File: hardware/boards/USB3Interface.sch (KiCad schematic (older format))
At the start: 6 parts, among them J2 USB3_Micro_B_Amphenol, U1 ECP5UM5G-381caBGA, U3 CYUSB3014, U6 128MiB

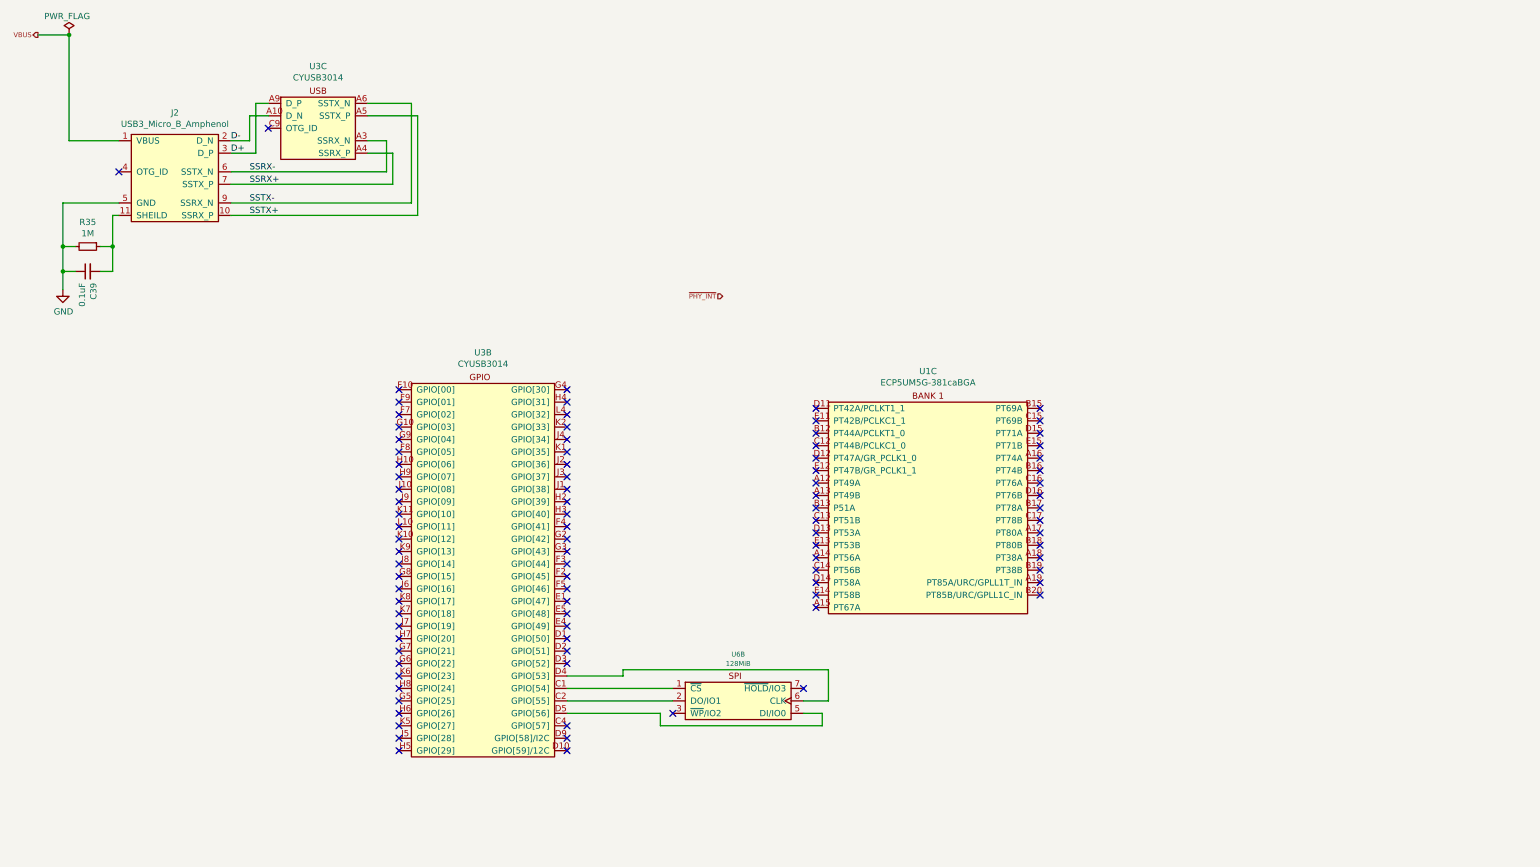
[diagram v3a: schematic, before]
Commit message: Added headers for the SPI flash for both the FPGA and the PHY
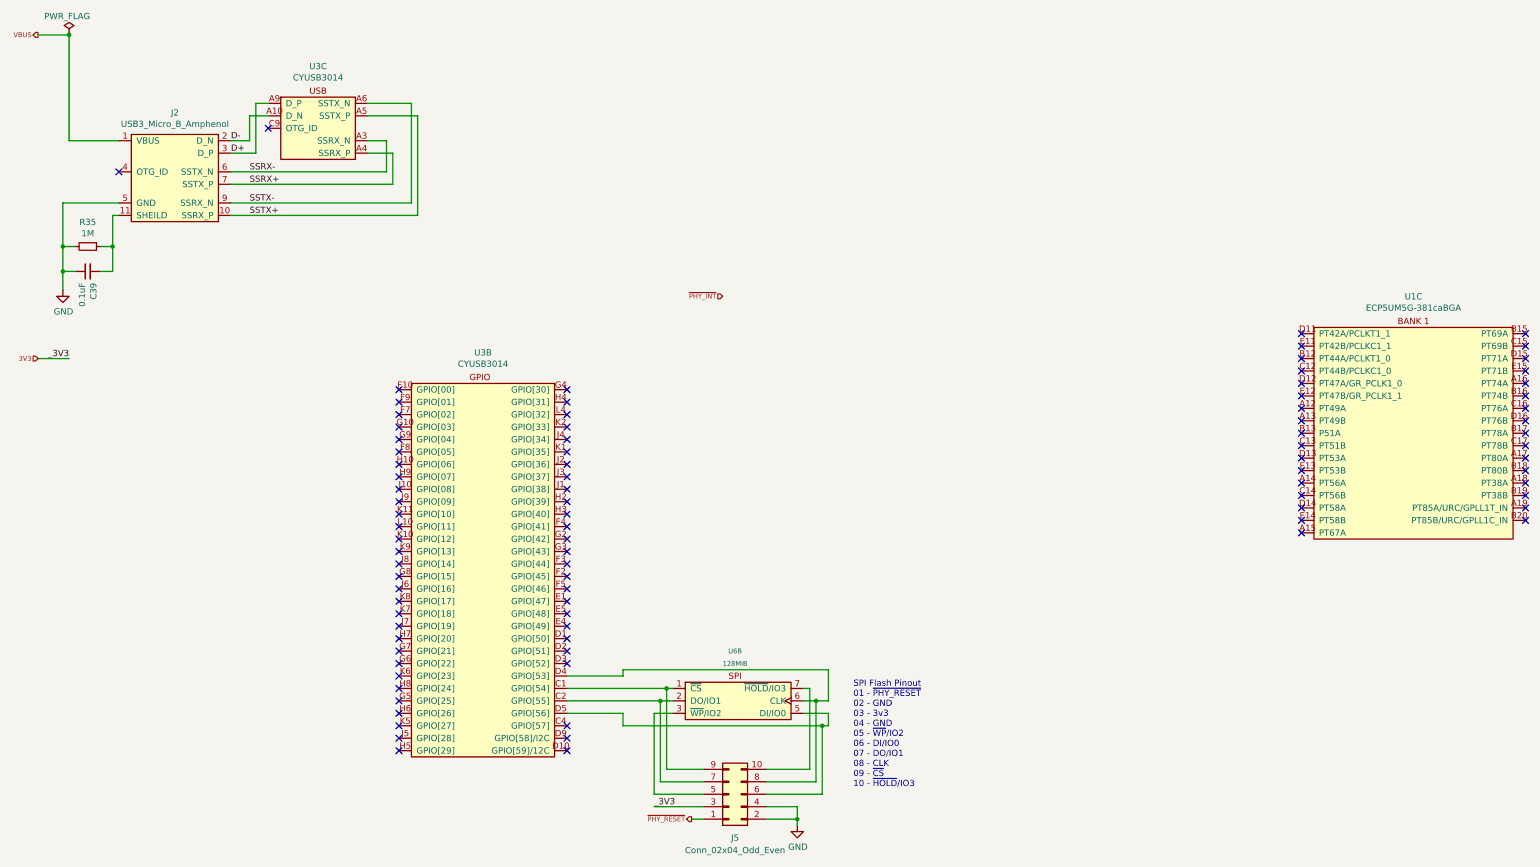
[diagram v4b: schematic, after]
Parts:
- added J5: Conn_02x04_Odd_Even, Connector_PinHeader_1.27mm:PinHeader_2x05_P1.27mm_Vertical, symbol Connector_Generic:Conn_02x05_Odd_Even
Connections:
- net GND: now also J5.2 (Pin_2), J5.4 (Pin_4)
- net at U3.C1 (GPIO[54]), U6.1 (~CS): now also J5.9 (Pin_9)
- net at U3.C2 (GPIO[55]), U6.2 (DO/IO1): now also J5.7 (Pin_7)
- net at U3.D4 (GPIO[53]), U6.6 (CLK): now also J5.8 (Pin_8)
- net at U3.D5 (GPIO[56]), U6.5 (DI/IO0): now also J5.6 (Pin_6)
- net at U6.3 (~WP~/IO2): now also J5.5 (Pin_5)
- net at U6.7 (~HOLD~/IO3): now also J5.10 (Pin_10)
- new net 3V3: J5.3 (Pin_3)
- new net ~PHY_RESET: J5.1 (Pin_1)
- no-connect marks 93 -> 91
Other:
- note added: "SPI Flash Pinout\n01 - ~PHY_RESET~\n02 - GND\n03 - 3v3\n04 - GND\n05 - ~WP~/IO2\n06 - DI/IO0\n07 - DO/IO1\n08 - CLK\n09 - ~CS~\n10 - ~HOLD~/IO3\n"
- moved on the sheet: U1C
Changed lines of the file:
@@
 L lethalbit:ECP5UM5G-381caBGA U?
 U 3 1 5F2EB784
-P 7950 3750
+P 11850 3150
 AR Path="/5F2EB784" Ref="U?"  Part="3"
 AR Path="/5F2CAFD2/5F2EB784" Ref="U1"  Part="3"
-F 0 "U1" H 7950 4098 50  0000 C CNN
-F 1 "ECP5UM5G-381caBGA" H 7950 4007 50  0000 C CNN
-F 2 "lethalbit:318caBGA" H 6600 3900 50  0001 C CNN
-F 3 "" H 6600 3900 50  0001 C CNN
-F 4 "Lattice" H 7950 3750 50  0001 C CNN "MFR"
-F 5 "LFE5UM5G-85F-8BG381I" H 7950 3750 50  0001 C CNN "MPN"
-F 6 "220-2112-ND" H 7950 3750 50  0001 C CNN "DIGIKEY_PN"
-	3    7950 3750
+F 0 "U1" H 11850 3498 50  0000 C CNN
+F 1 "ECP5UM5G-381caBGA" H 11850 3407 50  0000 C CNN
+F 2 "lethalbit:318caBGA" H 10500 3300 50  0001 C CNN
+F 3 "" H 10500 3300 50  0001 C CNN
+F 4 "Lattice" H 11850 3150 50  0001 C CNN "MFR"
+F 5 "LFE5UM5G-85F-8BG381I" H 11850 3150 50  0001 C CNN "MPN"
+F 6 "220-2112-ND" H 11850 3150 50  0001 C CNN "DIGIKEY_PN"
+	3    11850 3150
 	1    0    0    -1
 $EndComp
@@
 NoConn ~ 5050 3650
 NoConn ~ 5050 3550
-NoConn ~ 7050 3700
-NoConn ~ 7050 3800
-NoConn ~ 7050 3900
-NoConn ~ 7050 4000
-NoConn ~ 7050 4100
-NoConn ~ 7050 4200
-NoConn ~ 7050 4300
-NoConn ~ 7050 4400
-NoConn ~ 7050 4500
-NoConn ~ 7050 4600
-NoConn ~ 7050 4800
-NoConn ~ 7050 4900
-NoConn ~ 7050 5000
-NoConn ~ 7050 5100
-NoConn ~ 7050 5200
-NoConn ~ 7050 5300
-NoConn ~ 8850 5200
-NoConn ~ 8850 5100
-NoConn ~ 8850 5000
-NoConn ~ 8850 4900
-NoConn ~ 8850 4800
-NoConn ~ 8850 4700
-NoConn ~ 8850 4600
-NoConn ~ 8850 4500
-NoConn ~ 8850 4400
-NoConn ~ 8850 4300
-NoConn ~ 8850 4200
-NoConn ~ 8850 4100
-NoConn ~ 8850 4000
-NoConn ~ 8850 3900
-NoConn ~ 8850 3800
-NoConn ~ 8850 3700
+NoConn ~ 10950 3100
+NoConn ~ 10950 3200
+NoConn ~ 10950 3300
+NoConn ~ 10950 3400
+NoConn ~ 10950 3500
+NoConn ~ 10950 3600
+NoConn ~ 10950 3700
+NoConn ~ 10950 3800
+NoConn ~ 10950 3900
+NoConn ~ 10950 4000
+NoConn ~ 10950 4200
+NoConn ~ 10950 4300
+NoConn ~ 10950 4400
+NoConn ~ 10950 4500
+NoConn ~ 10950 4600
+NoConn ~ 10950 4700
+NoConn ~ 12750 4600
+NoConn ~ 12750 4500
+NoConn ~ 12750 4400
+NoConn ~ 12750 4300
+NoConn ~ 12750 4200
+NoConn ~ 12750 4100
+NoConn ~ 12750 4000
+NoConn ~ 12750 3900
+NoConn ~ 12750 3800
+NoConn ~ 12750 3700
+NoConn ~ 12750 3600
+NoConn ~ 12750 3500
+NoConn ~ 12750 3400
+NoConn ~ 12750 3300
+NoConn ~ 12750 3200
+NoConn ~ 12750 3100
 Text HLabel 800  700  0    39   Output ~ 0
 VBUS
@@
 Wire Wire Line
 	3850 1350 3450 1350
-NoConn ~ 7050 4700
+NoConn ~ 10950 4100
 Text Label 2500 1800 0    50   ~ 0
 SSRX-
@@
 AR Path="/5EF66251/5FF1D42C" Ref="U?"  Part="2"
 AR Path="/5F2CAFD2/5FF1D42C" Ref="U6"  Part="2"
-F 0 "U6" H 6425 6124 39  0000 C CNN
-F 1 "128MiB" H 6425 6049 39  0000 C CNN
+F 0 "U6" H 6400 6150 39  0000 C CNN
+F 1 "128MiB" H 6400 6050 39  0000 C CNN
 F 2 "lethalbit-memory:WSON-8-1EP-6.0x8.0mm" H 6400 6050 39  0001 C CNN
 F 3 "https://www.winbond.com/resource-files/w25n01gv%20revl%20050918%20unsecured.pdf" H 6400 6050 39  0001 C CNN
@@
 $EndComp
 Wire Wire Line
-	6950 6050 7150 6050
+	6950 6050 7050 6050
 Wire Wire Line
 	7150 6050 7150 5800
@@
 	5500 5850 5050 5850
 Wire Wire Line
-	5900 5950 5050 5950
-Wire Wire Line
-	5900 6050 5050 6050
-Wire Wire Line
-	6950 6150 7100 6150
-Wire Wire Line
-	7100 6150 7100 6250
-Wire Wire Line
-	7100 6250 5800 6250
-Wire Wire Line
-	5800 6250 5800 6150
-Wire Wire Line
-	5800 6150 5050 6150
+	5900 5950 5850 5950
+Wire Wire Line
+	5900 6050 5800 6050
+Wire Wire Line
+	6950 6150 7150 6150
+Wire Wire Line
+	7150 6150 7150 6250
+Wire Wire Line
+	7150 6250 7100 6250
+Wire Wire Line
+	5500 6250 5500 6150
+Wire Wire Line
+	5500 6150 5050 6150
 $Comp
 L power:PWR_FLAG #FLG?
@@
 $EndComp
 Connection ~ 1050 700
-NoConn ~ 6950 5950
-NoConn ~ 5900 6150
 Text HLabel 6300 2800 0    39   Input ~ 0
 ~PHY_INT
+$Comp
+L Connector_Generic:Conn_02x05_Odd_Even J?
+U 1 1 60F06E66
+P 6350 6800
+AR Path="/5EF66251/60F06E66" Ref="J?"  Part="1"
+AR Path="/5F2CAFD2/60F06E66" Ref="J5"  Part="1"
+F 0 "J5" H 6400 7150 50  0000 C CNN
+F 1 "Conn_02x04_Odd_Even" H 6400 7250 50  0000 C CNN
+F 2 "Connector_PinHeader_1.27mm:PinHeader_2x05_P1.27mm_Vertical" H 6350 6800 50  0001 C CNN
+F 3 "~" H 6350 6800 50  0001 C CNN
+	1    6350 6800
+	1    0    0    1
+$EndComp
+Text Notes 7350 6750 0    50   ~ 0
+SPI Flash Pinout\n01 - ~PHY_RESET~\n02 - GND\n03 - 3v3\n04 - GND\n05 - ~WP~/IO2\n06 - DI/IO0\n07 - DO/IO1\n08 - CLK\n09 - ~CS~\n10 - ~HOLD~/IO3\n
+$Comp
+L power:GND #PWR0138
+U 1 1 60F24716
+P 6900 7050
+F 0 "#PWR0138" H 6900 6800 50  0001 C CNN
+F 1 "GND" H 6905 6877 50  0000 C CNN
+F 2 "" H 6900 7050 50  0001 C CNN
+F 3 "" H 6900 7050 50  0001 C CNN
+	1    6900 7050
+	1    0    0    -1
+$EndComp
+Text HLabel 6050 7000 0    39   Output ~ 0
+~PHY_RESET
+Wire Wire Line
+	6950 5950 7000 5950
+Wire Wire Line
+	7000 5950 7000 6600
+Wire Wire Line
+	7000 6600 6650 6600
+Wire Wire Line
+	7050 6050 7050 6700
+Wire Wire Line
+	7050 6700 6650 6700
+Connection ~ 7050 6050
+Wire Wire Line
+	7050 6050 7150 6050
+Wire Wire Line
+	7100 6250 7100 6800
+Wire Wire Line
+	7100 6800 6650 6800
+Connection ~ 7100 6250
+Wire Wire Line
+	7100 6250 5500 6250
+Wire Wire Line
+	6150 6600 5850 6600
+Wire Wire Line
+	5850 6600 5850 5950
+Connection ~ 5850 5950
+Wire Wire Line
+	5850 5950 5050 5950
+Wire Wire Line
+	5800 6050 5800 6700
+Wire Wire Line
+	5800 6700 6150 6700
+Connection ~ 5800 6050
+Wire Wire Line
+	5800 6050 5050 6050
+Wire Wire Line
+	5900 6150 5750 6150
+Wire Wire Line
+	5750 6150 5750 6800
+Wire Wire Line
+	5750 6800 6150 6800
+Wire Wire Line
+	6050 7000 6150 7000
+Wire Wire Line
+	6650 6900 6900 6900
+Wire Wire Line
+	6900 6900 6900 7000
+Wire Wire Line
+	6650 7000 6900 7000
+Connection ~ 6900 7000
+Wire Wire Line
+	6900 7000 6900 7050
+Wire Wire Line
+	6150 6900 5750 6900
+Text Label 5750 6900 0    50   ~ 0
+_3V3
+Text HLabel 800  3300 0    39   Input ~ 0
+3V3
+Wire Wire Line
+	800  3300 1050 3300
+Text Label 1050 3300 2    50   ~ 0
+_3V3
 $EndSCHEMATC

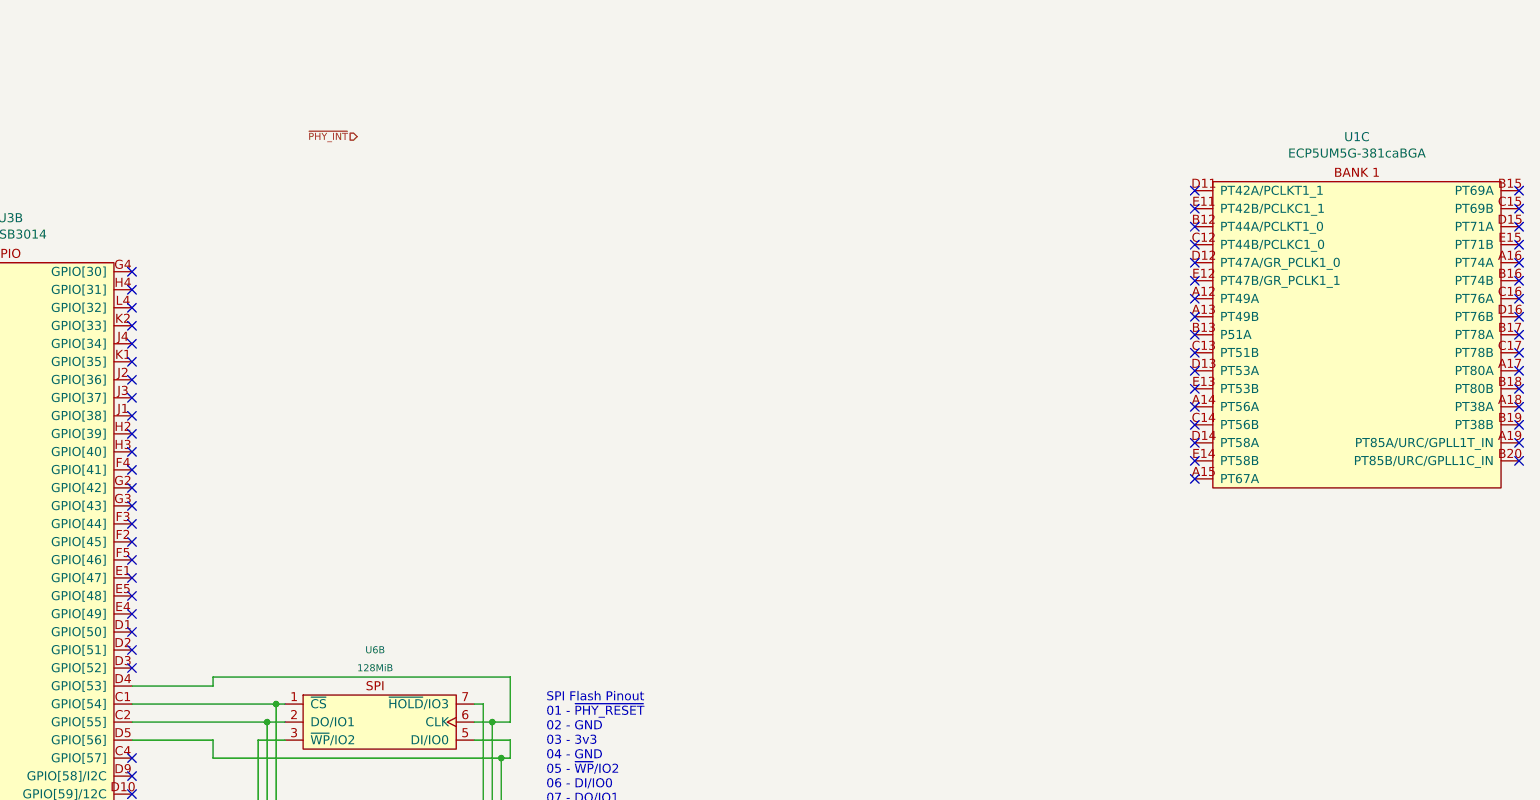
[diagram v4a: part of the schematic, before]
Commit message: Added the main OSC for the FPGA
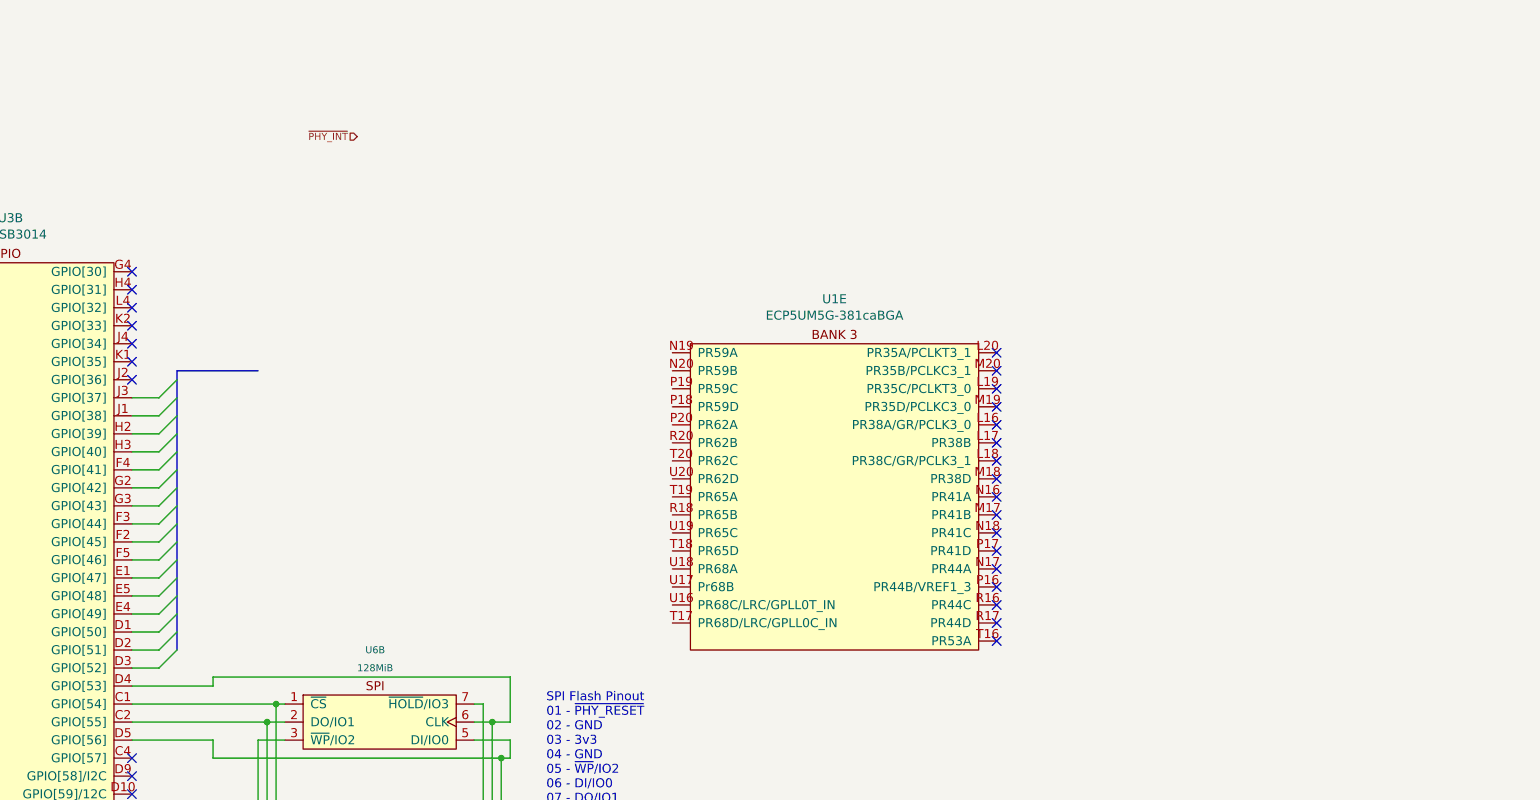
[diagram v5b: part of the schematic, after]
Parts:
- removed U1: ECP5UM5G-381caBGA, lethalbit:318caBGA, symbol lethalbit:ECP5UM5G-381caBGA
- added U1: ECP5UM5G-381caBGA, lethalbit:318caBGA, symbol lethalbit:ECP5UM5G-381caBGA
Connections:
- no-connect marks 91 -> 59
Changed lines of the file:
@@
 $EndDescr
-$Comp
-L lethalbit:ECP5UM5G-381caBGA U?
-U 3 1 5F2EB784
-P 11850 3150
-AR Path="/5F2EB784" Ref="U?"  Part="3"
-AR Path="/5F2CAFD2/5F2EB784" Ref="U1"  Part="3"
-F 0 "U1" H 11850 3498 50  0000 C CNN
-F 1 "ECP5UM5G-381caBGA" H 11850 3407 50  0000 C CNN
-F 2 "lethalbit:318caBGA" H 10500 3300 50  0001 C CNN
-F 3 "" H 10500 3300 50  0001 C CNN
-F 4 "Lattice" H 11850 3150 50  0001 C CNN "MFR"
-F 5 "LFE5UM5G-85F-8BG381I" H 11850 3150 50  0001 C CNN "MPN"
-F 6 "220-2112-ND" H 11850 3150 50  0001 C CNN "DIGIKEY_PN"
-	3    11850 3150
-	1    0    0    -1
-$EndComp
 $Comp
 L lethalbit:CYUSB3014 U3
@@
 NoConn ~ 5050 6350
 NoConn ~ 5050 6250
-NoConn ~ 5050 5750
-NoConn ~ 5050 5650
-NoConn ~ 5050 5550
-NoConn ~ 5050 5450
-NoConn ~ 5050 5350
-NoConn ~ 5050 5250
-NoConn ~ 5050 5150
-NoConn ~ 5050 5050
-NoConn ~ 5050 4950
-NoConn ~ 5050 4850
-NoConn ~ 5050 4750
-NoConn ~ 5050 4650
-NoConn ~ 5050 4550
-NoConn ~ 5050 4450
-NoConn ~ 5050 4350
-NoConn ~ 5050 4250
 NoConn ~ 5050 4150
 NoConn ~ 5050 4050
 NoConn ~ 5050 3950
 NoConn ~ 5050 3850
-NoConn ~ 5050 3750
-NoConn ~ 5050 3650
-NoConn ~ 5050 3550
-NoConn ~ 10950 3100
-NoConn ~ 10950 3200
-NoConn ~ 10950 3300
-NoConn ~ 10950 3400
-NoConn ~ 10950 3500
-NoConn ~ 10950 3600
-NoConn ~ 10950 3700
-NoConn ~ 10950 3800
-NoConn ~ 10950 3900
-NoConn ~ 10950 4000
-NoConn ~ 10950 4200
-NoConn ~ 10950 4300
-NoConn ~ 10950 4400
-NoConn ~ 10950 4500
-NoConn ~ 10950 4600
-NoConn ~ 10950 4700
-NoConn ~ 12750 4600
-NoConn ~ 12750 4500
-NoConn ~ 12750 4400
-NoConn ~ 12750 4300
-NoConn ~ 12750 4200
-NoConn ~ 12750 4100
-NoConn ~ 12750 4000
-NoConn ~ 12750 3900
-NoConn ~ 12750 3800
-NoConn ~ 12750 3700
-NoConn ~ 12750 3600
-NoConn ~ 12750 3500
-NoConn ~ 12750 3400
-NoConn ~ 12750 3300
-NoConn ~ 12750 3200
-NoConn ~ 12750 3100
+NoConn ~ 9850 5600
+NoConn ~ 9850 5500
+NoConn ~ 9850 5400
+NoConn ~ 9850 5300
+NoConn ~ 9850 5200
+NoConn ~ 9850 5100
+NoConn ~ 9850 5000
+NoConn ~ 9850 4900
+NoConn ~ 9850 4800
+NoConn ~ 9850 4700
+NoConn ~ 9850 4600
+NoConn ~ 9850 4500
+NoConn ~ 9850 4400
+NoConn ~ 9850 4300
+NoConn ~ 9850 4200
+NoConn ~ 9850 4100
+NoConn ~ 9850 4000
 Text HLabel 800  700  0    39   Output ~ 0
 VBUS
@@
 Wire Wire Line
 	3850 1350 3450 1350
-NoConn ~ 10950 4100
 Text Label 2500 1800 0    50   ~ 0
 SSRX-
@@
 Text Label 1050 3300 2    50   ~ 0
 _3V3
+NoConn ~ 5050 3750
+NoConn ~ 5050 3650
+NoConn ~ 5050 3550
+Entry Wire Line
+	5200 5750 5300 5650
+Entry Wire Line
+	5200 5650 5300 5550
+Entry Wire Line
+	5200 5550 5300 5450
+Entry Wire Line
+	5200 5450 5300 5350
+Entry Wire Line
+	5200 5350 5300 5250
+Entry Wire Line
+	5200 5250 5300 5150
+Entry Wire Line
+	5200 5150 5300 5050
+Entry Wire Line
+	5200 5050 5300 4950
+Entry Wire Line
+	5200 4950 5300 4850
+Entry Wire Line
+	5200 4850 5300 4750
+Entry Wire Line
+	5200 4750 5300 4650
+Entry Wire Line
+	5200 4650 5300 4550
+Entry Wire Line
+	5200 4550 5300 4450
+Entry Wire Line
+	5200 4450 5300 4350
+Entry Wire Line
+	5200 4350 5300 4250
+Entry Wire Line
+	5200 4250 5300 4150
+Wire Wire Line
+	5050 4250 5200 4250
+Wire Wire Line
+	5050 4350 5200 4350
+Wire Wire Line
+	5050 4450 5200 4450
+Wire Wire Line
+	5050 4550 5200 4550
+Wire Wire Line
+	5050 4650 5200 4650
+Wire Wire Line
+	5050 4750 5200 4750
+Wire Wire Line
+	5050 4850 5200 4850
+Wire Wire Line
+	5050 4950 5200 4950
+Wire Wire Line
+	5050 5050 5200 5050
+Wire Wire Line
+	5050 5150 5200 5150
+Wire Wire Line
+	5050 5250 5200 5250
+Wire Wire Line
+	5050 5350 5200 5350
+Wire Wire Line
+	5050 5450 5200 5450
+Wire Wire Line
+	5050 5550 5200 5550
+Wire Wire Line
+	5050 5650 5200 5650
+Wire Wire Line
+	5050 5750 5200 5750
+Wire Bus Line
+	5300 4100 5750 4100
+Wire Bus Line
+	5300 4100 5300 5650
+$Comp
+L lethalbit:ECP5UM5G-381caBGA U?
+U 5 1 610C217C
+P 8950 4050
+AR Path="/5EF67D90/610C217C" Ref="U?"  Part="5"
+AR Path="/5F2CAFD2/610C217C" Ref="U1"  Part="5"
+F 0 "U1" H 8950 4398 50  0000 C CNN
+F 1 "ECP5UM5G-381caBGA" H 8950 4307 50  0000 C CNN
+F 2 "lethalbit:318caBGA" H 7600 4200 50  0001 C CNN
+F 3 "" H 7600 4200 50  0001 C CNN
+F 4 "Lattice" H 8950 4050 50  0001 C CNN "MFR"
+F 5 "LFE5UM5G-85F-8BG381I" H 8950 4050 50  0001 C CNN "MPN"
+F 6 "220-2112-ND" H 8950 4050 50  0001 C CNN "DIGIKEY_PN"
+	5    8950 4050
+	-1   0    0    -1
+$EndComp
 $EndSCHEMATC
